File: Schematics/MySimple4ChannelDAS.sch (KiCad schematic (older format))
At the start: 25 parts, among them J1 Conn_01x02_Male, J2 Conn_01x02_Male, J3 Conn_01x02_Male, J4 Conn_01x02_Male, J5 Conn_01x02_Male, J6 Conn_01x02_Male, J7 Conn_01x02_Male, J8 Conn_01x02_Male, J9 Conn_01x02_Male, U1 LM324A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

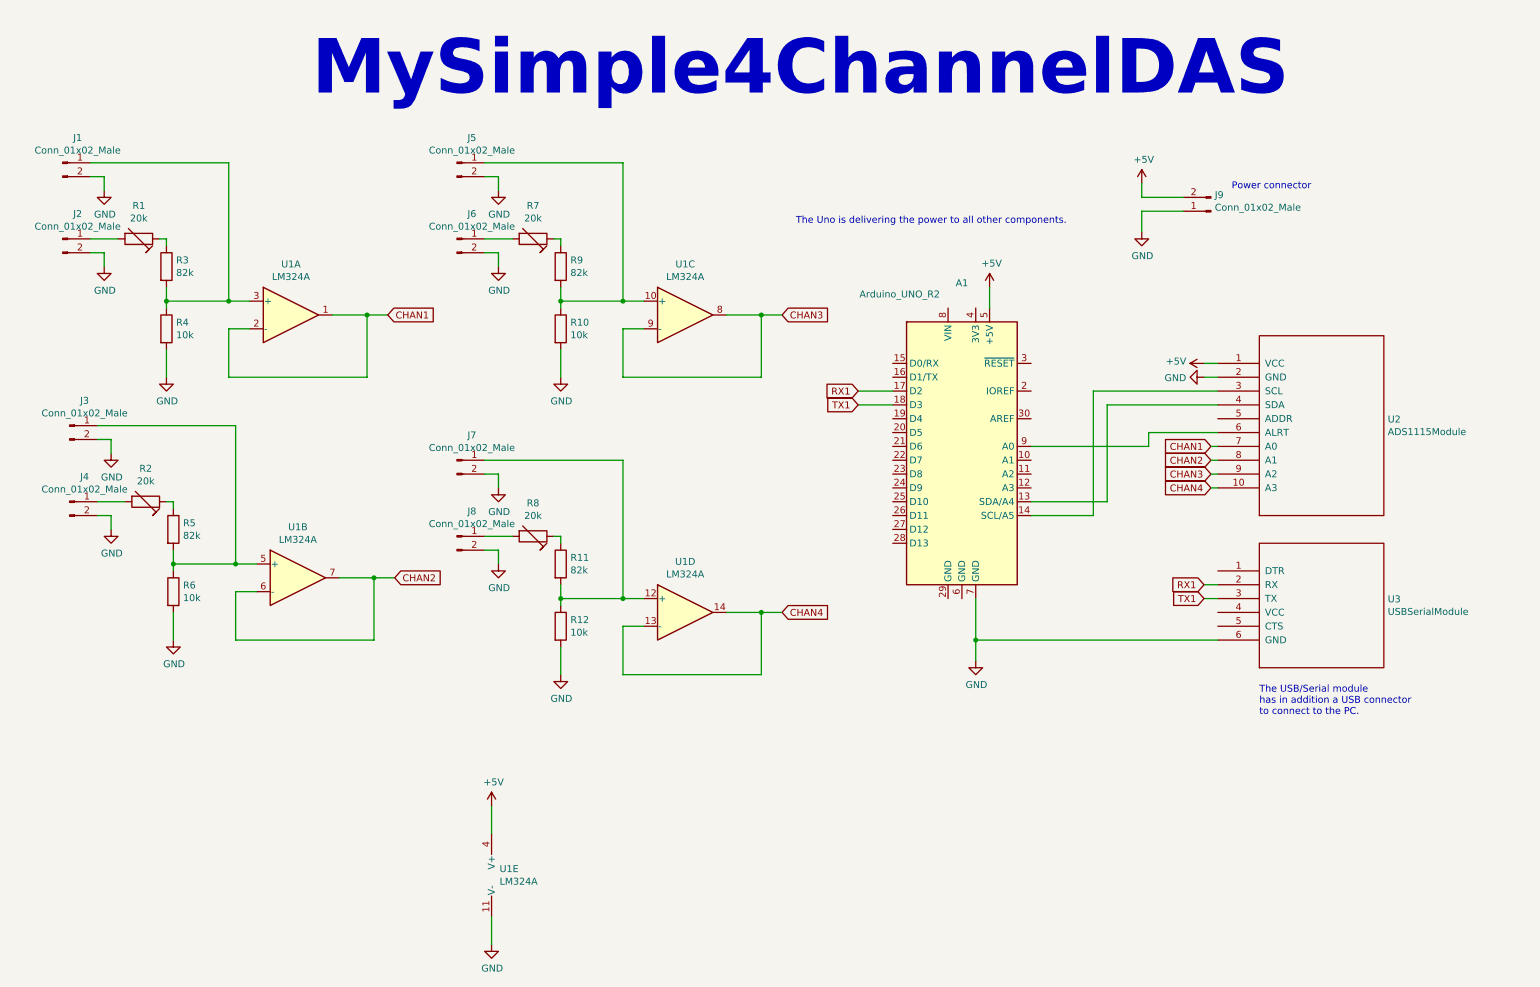
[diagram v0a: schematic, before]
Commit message: updated schematics
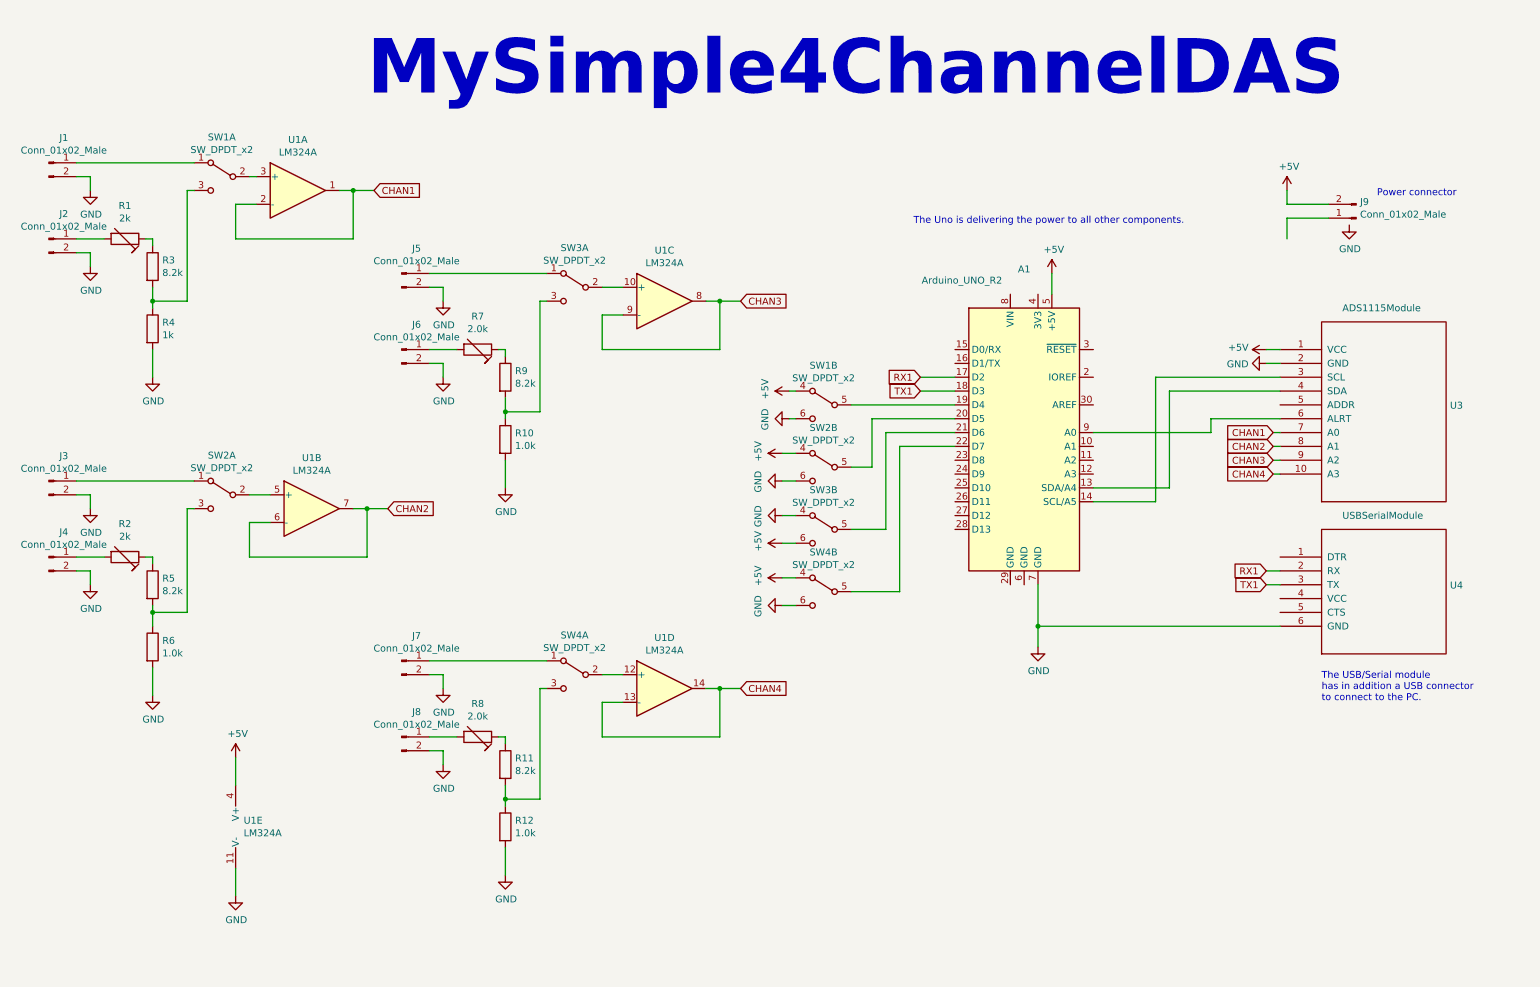
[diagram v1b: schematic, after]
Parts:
- added SW1, SW2, SW3, SW4: SW_DPDT_x2, symbol Switch:SW_DPDT_x2
- R1, R2: value 20k -> 2k
- R10, R12, R6: value 10k -> 1.0k
- R11, R3, R5, R9: value 82k -> 8.2k
- R4: value 10k -> 1k
- R7, R8: value 20k -> 2.0k
- renumbered U2 to U3, U3 to U4
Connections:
- net +5V: now also SW1.4 (A), SW2.4 (A), SW3.6 (C), SW4.4 (A)
- net GND: now also SW1.6 (C), SW2.6 (C), SW3.4 (A), SW4.6 (C); no longer J9.1 (Pin_1)
- net at R3.2, R4.1: now also SW1.3 (C); no longer J1.1 (Pin_1), U1.3 (+)
- net at R5.2, R6.1: now also SW2.3 (C); no longer J3.1 (Pin_1), U1.5 (+)
- net at R10.1, R9.2: now also SW3.3 (C); no longer J5.1 (Pin_1), U1.10 (+)
- net at R11.2, R12.1: now also SW4.3 (C); no longer J7.1 (Pin_1), U1.12 (+)
- net at A1.19 (D4): now also SW1.5 (B)
- net at A1.20 (D5): now also SW2.5 (B)
- net at A1.21 (D6): now also SW3.5 (B)
- net at A1.22 (D7): now also SW4.5 (B)
- new net: SW1.2 (B), U1.3 (+)
- new net: SW2.2 (B), U1.5 (+)
- new net: SW3.2 (B), U1.10 (+)
- new net: SW4.2 (B), U1.12 (+)
- new net: J1.1 (Pin_1), SW1.1 (A)
- new net: J3.1 (Pin_1), SW2.1 (A)
- new net: J5.1 (Pin_1), SW3.1 (A)
- new net: J7.1 (Pin_1), SW4.1 (A)
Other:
- moved on the sheet: A1, J1, J2, J3, J4, J5, J6, J7, J8, J9, R1, R10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

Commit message: added processing of switches
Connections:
- net at A1.19 (D4): no longer SW1.5 (B)
- net at A1.20 (D5): no longer SW2.5 (B)
- net at A1.21 (D6): no longer SW3.5 (B)
- net at A1.22 (D7): no longer SW4.5 (B)
- net at A1.23 (D8): now also SW4.5 (B)
- net at A1.24 (D9): now also SW3.5 (B)
- net at A1.25 (D10): now also SW2.5 (B)
- net at A1.26 (D11): now also SW1.5 (B)
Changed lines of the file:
@@
 Wire Wire Line
 	6100 3450 6150 3450
-Wire Wire Line
-	6550 3350 7300 3350
 $Comp
 L power:GND #PWR08
@@
 	6050 4800 6150 4800
 Wire Wire Line
-	6550 3800 6700 3800
+	7300 3750 7200 3750
 Wire Wire Line
-	6700 3800 6700 3450
+	7200 3750 7200 4700
 Wire Wire Line
-	6700 3450 7300 3450
+	6550 4700 7200 4700
 Wire Wire Line
-	6550 4250 6800 4250
+	7100 4250 7100 3850
 Wire Wire Line
-	6800 4250 6800 3550
+	7100 3850 7300 3850
 Wire Wire Line
-	6800 3550 7300 3550
+	6550 4250 7100 4250
 Wire Wire Line
-	6550 4700 6900 4700
+	7000 3800 7000 3950
 Wire Wire Line
-	6900 4700 6900 3650
+	7000 3950 7300 3950
 Wire Wire Line
-	6900 3650 7300 3650
+	6550 3800 7000 3800
+Wire Wire Line
+	6550 3350 6900 3350
+Wire Wire Line
+	6900 3350 6900 4050
+Wire Wire Line
+	6900 4050 7300 4050
 $EndSCHEMATC
